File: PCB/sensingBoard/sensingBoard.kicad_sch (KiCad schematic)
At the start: 37 parts, among them J1 Conn_01x02_Socket, J2 Conn_01x03_Socket, J4 Conn_01x04_MountingPin, P1 USB_C_Plug_USB2.0, SW1 SW_Push, SW2 SW_Push, U1 AMS1117, U2 ESP32-C3-MINI-1, X1 32.768

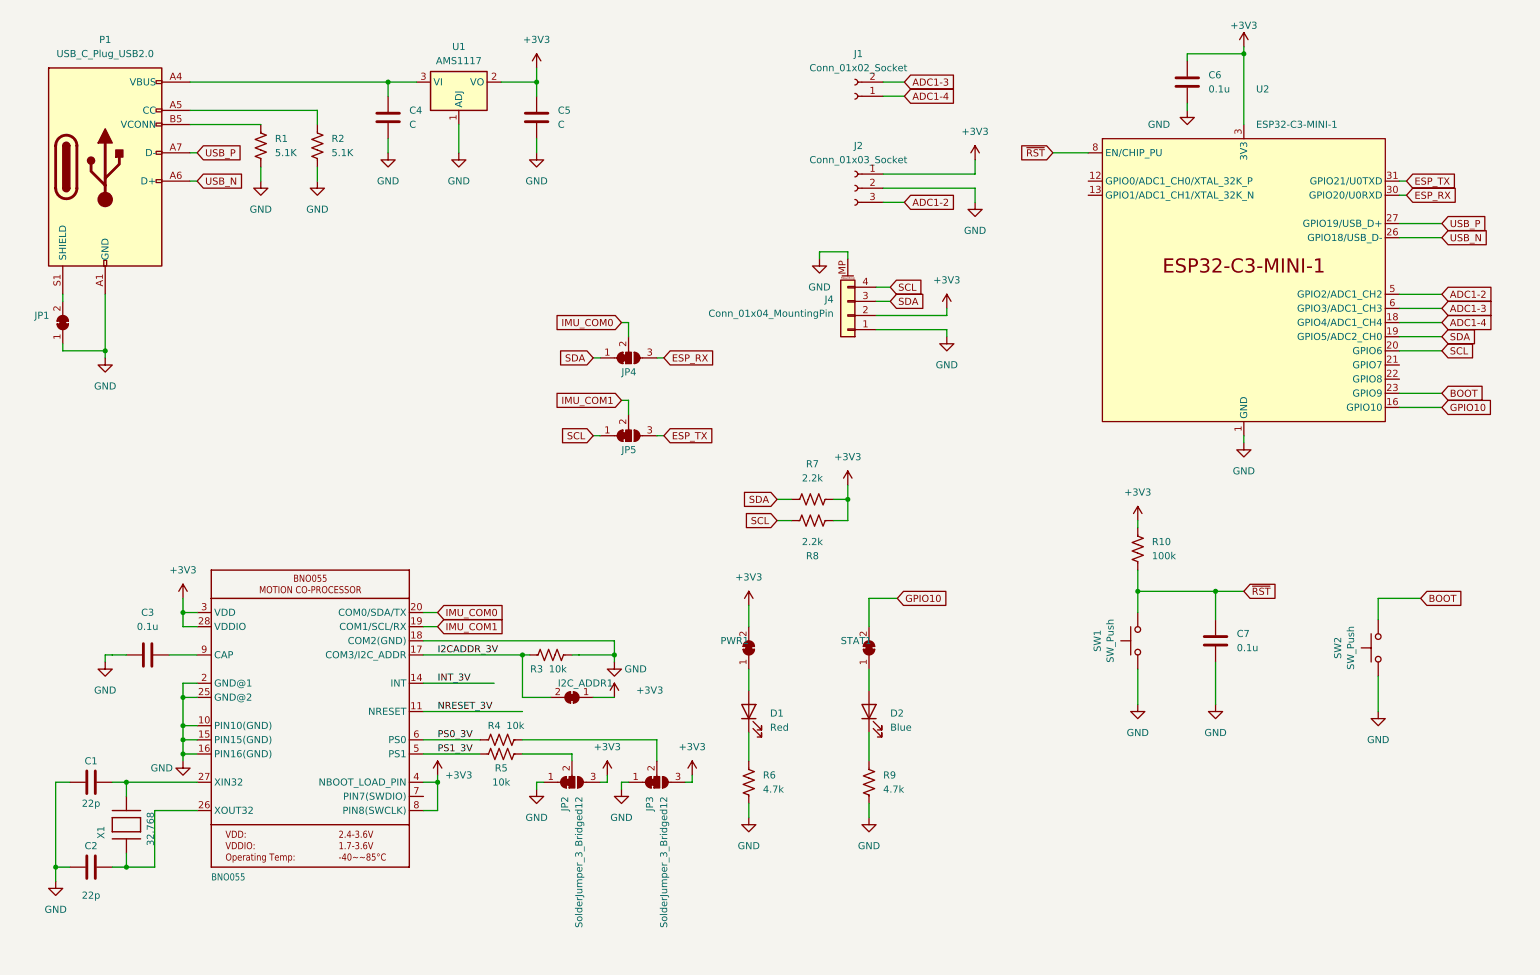
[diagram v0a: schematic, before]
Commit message: modified sensor board and wrote firmware for wireless data transfer
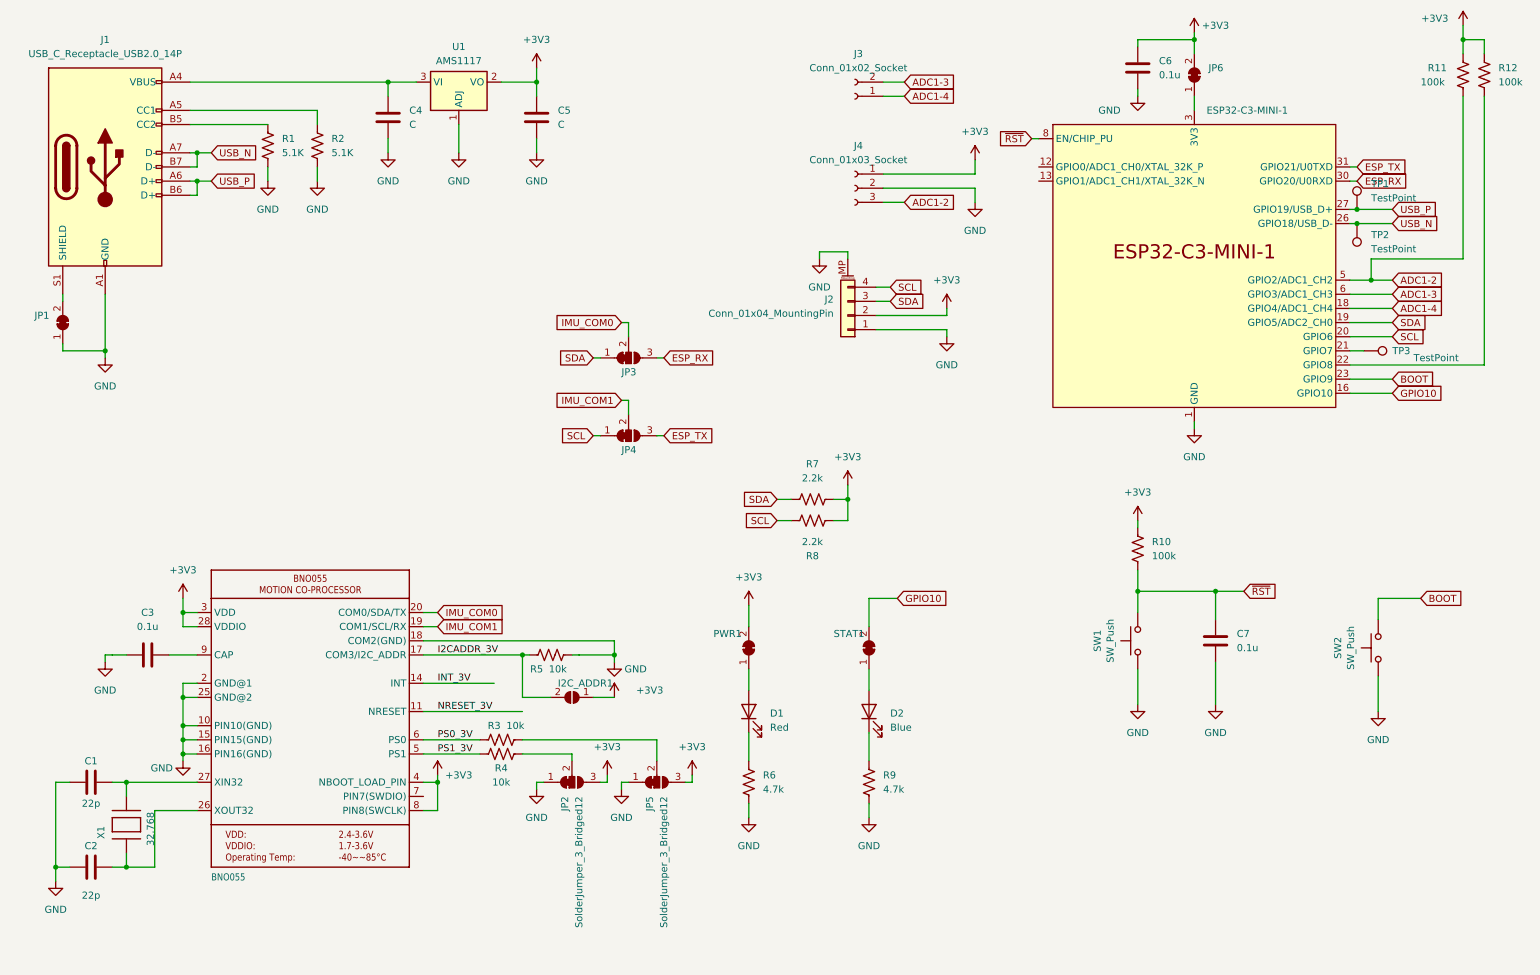
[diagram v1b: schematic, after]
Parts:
- removed P1: USB_C_Plug_USB2.0, Connector_USB:USB_C_Receptacle_GCT_USB4105-xx-A_16P_TopMnt_Horizontal, symbol Connector:USB_C_Plug_USB2.0
- added J1: USB_C_Receptacle_USB2.0_14P, Connector_USB:USB_C_Receptacle_GCT_USB4105-xx-A_16P_TopMnt_Horizontal, symbol Connector:USB_C_Receptacle_USB2.0_14P
- added JP6: ~, Jumper:SolderJumper-2_P1.3mm_Bridged_RoundedPad1.0x1.5mm, symbol Jumper:SolderJumper_2_Bridged
- added R11, R12: 100k, Resistor_SMD:R_0805_2012Metric_Pad1.20x1.40mm_HandSolder, symbol Device:R_US
- added TP1, TP2, TP3: TestPoint, TestPoint:TestPoint_Pad_D1.0mm, symbol Connector:TestPoint
- I2C_ADDR1: symbol Jumper:SolderJumper_2_Bridged -> Jumper:SolderJumper_2_Open
- JP1, PWR1, STAT1: footprint Jumper:SolderJumper-2_P1.3mm_Open_RoundedPad1.0x1.5mm -> Jumper:SolderJumper-2_P1.3mm_Bridged_RoundedPad1.0x1.5mm
- renumbered J4 to J2, J1 to J3, J2 to J4, JP4 to JP3, JP5 to JP4, JP3 to JP5, R4 to R3, R5 to R4, R3 to R5
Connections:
- net +3V3: now also JP6.2 (B), R11.1, R12.1; no longer U2.3 (3V3)
- net ADC1-2: now also R11.2
- net GND: now also J1.A1 (GND), J1.A12 (GND), J1.B1 (GND), J1.B12 (GND)
- net USB_N: now also J1.A7 (D-), J1.B7 (D-), TP2.1
- net USB_P: now also J1.A6 (D+), J1.B6 (D+), TP1.1
- net at C4.1, U1.3 (VI): now also J1.A4 (VBUS), J1.A9 (VBUS), J1.B4 (VBUS), J1.B9 (VBUS)
- net at R2.1: now also J1.A5 (CC1)
- net at R1.1: now also J1.B5 (CC2)
- net at JP1.2 (B): now also J1.S1 (SHIELD)
- net at U2.21 (GPIO7): now also TP3.1
- net at U2.22 (GPIO8): now also R12.2
- new net: JP6.1 (A), U2.3 (3V3)
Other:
- moved on the sheet: C6, R1

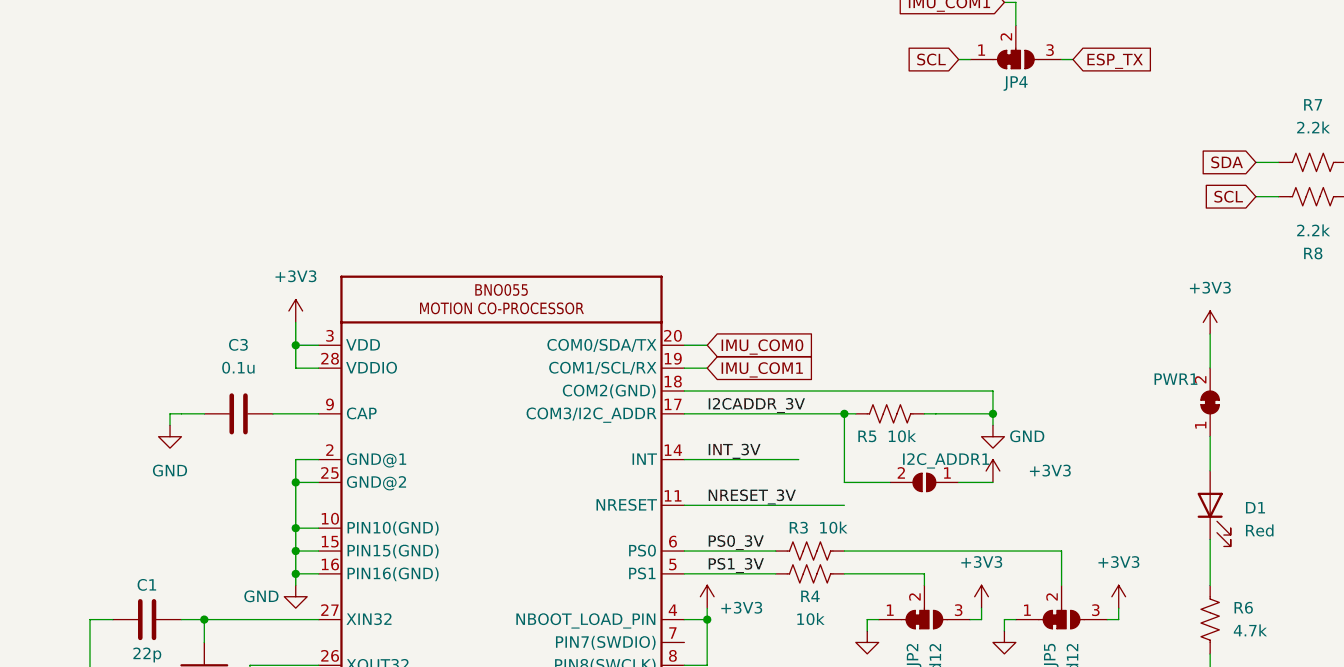
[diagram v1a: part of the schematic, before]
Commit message: gitignore for kicad backup, added pullup for nreset on imu
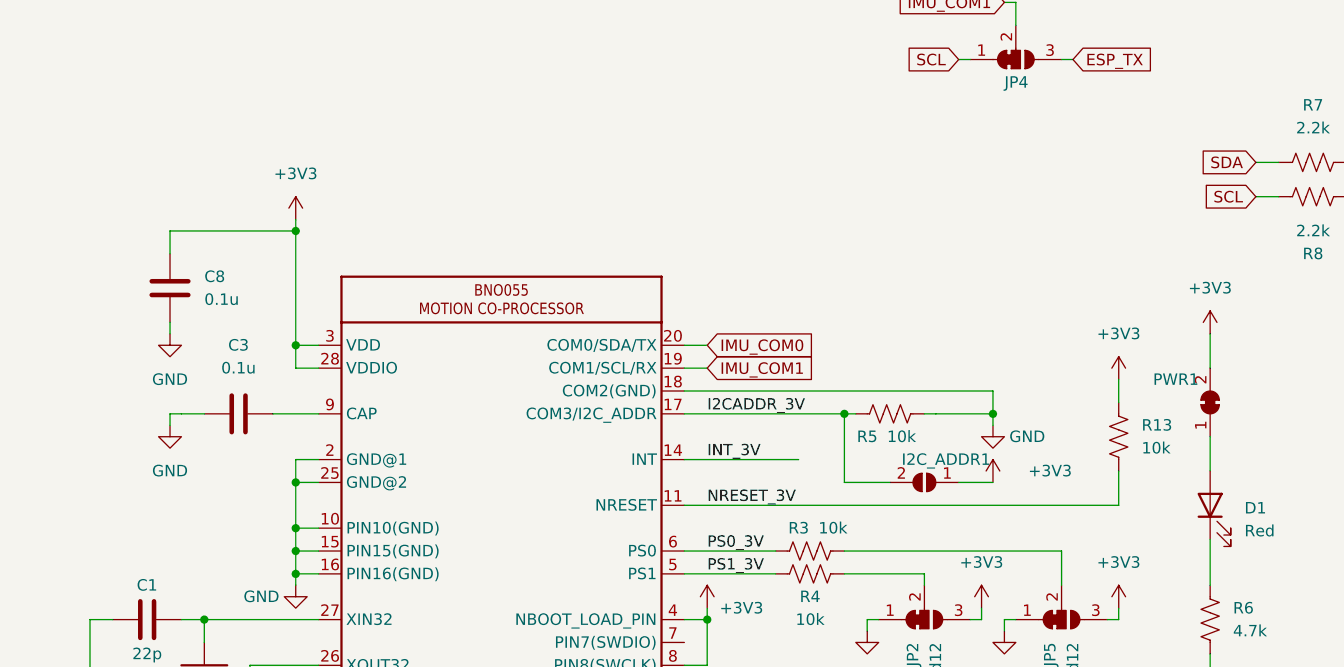
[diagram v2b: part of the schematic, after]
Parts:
- added C8: 0.1u, Capacitor_SMD:C_0805_2012Metric_Pad1.18x1.45mm_HandSolder, symbol Device:C
- added R13: 10k, Resistor_SMD:R_0805_2012Metric_Pad1.20x1.40mm_HandSolder, symbol Device:R_US
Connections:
- net +3V3: now also C8.1, R13.1
- net GND: now also C8.2
- net NRESET_3V: now also R13.2
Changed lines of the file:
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@@
   (junction (at 31.75 151.13) (diameter 0) (color 0 0 0 0)
   )
+  (junction (at 41.91 107.95) (diameter 0) (color 0 0 0 0)
+  )
   (junction (at 44.45 38.1) (diameter 0) (color 0 0 0 0)
   )
@@
     (stroke (width 0) (type default))
   )
+  (wire (pts (xy 27.94 107.95) (xy 41.91 107.95))
+    (stroke (width 0) (type default))
+  )
   (wire (pts (xy 87.63 156.21) (xy 85.09 156.21))
     (stroke (width 0.1524) (type solid))
@@
     (stroke (width 0) (type default))
   )
+  (wire (pts (xy 133.35 124.46) (xy 133.35 127))
+    (stroke (width 0) (type default))
+  )
   (wire (pts (xy 213.36 116.84) (xy 227.33 116.84))
     (stroke (width 0) (type default))
@@
     (stroke (width 0) (type default))
   )
+  (wire (pts (xy 41.91 107.95) (xy 41.91 106.68))
+    (stroke (width 0.1524) (type solid))
+  )
   (wire (pts (xy 44.45 135.89) (xy 41.91 135.89))
     (stroke (width 0.1524) (type solid))
@@
     (stroke (width 0) (type default))
   )
+  (wire (pts (xy 27.94 118.11) (xy 27.94 119.38))
+    (stroke (width 0) (type default))
+  )
   (wire (pts (xy 41.91 146.05) (xy 41.91 147.32))
     (stroke (width 0) (type default))
@@
     (stroke (width 0.1524) (type solid))
   )
+  (wire (pts (xy 133.35 134.62) (xy 133.35 138.43))
+    (stroke (width 0.1524) (type solid))
+  )
   (wire (pts (xy 44.45 146.05) (xy 41.91 146.05))
     (stroke (width 0.1524) (type solid))
@@
     (stroke (width 0) (type default))
   )
+  (wire (pts (xy 27.94 107.95) (xy 27.94 110.49))
+    (stroke (width 0) (type default))
+  )
   (wire (pts (xy 78.74 25.4) (xy 78.74 27.94))
     (stroke (width 0) (type default))
@@
     (stroke (width 0.1524) (type solid))
   )
-  (wire (pts (xy 41.91 120.65) (xy 41.91 118.11))
+  (wire (pts (xy 41.91 120.65) (xy 41.91 107.95))
     (stroke (width 0.1524) (type solid))
   )
@@
     (stroke (width 0) (type default))
   )
-  (wire (pts (xy 85.09 138.43) (xy 102.87 138.43))
+  (wire (pts (xy 85.09 138.43) (xy 133.35 138.43))
     (stroke (width 0.1524) (type solid))
   )
@@
         (path "/393f72fc-5c48-49dc-87e0-7e68fe660379"
           (reference "#PWR028") (unit 1)
+        )
+      )
+    )
+  )
+  (symbol (lib_id "Device:C") (at 27.94 114.3 0) (unit 1)
+    (in_bom yes) (on_board yes) (dnp no) (fields_autoplaced)
+    (property "Reference" "C8" (at 31.75 113.03 0)
+      (effects (font (size 1.27 1.27)) (justify left))
+    )
+    (property "Value" "0.1u" (at 31.75 115.57 0)
+      (effects (font (size 1.27 1.27)) (justify left))
+    )
+    (property "Footprint" "Capacitor_SMD:C_0805_2012Metric_Pad1.18x1.45mm_HandSolder" (at 28.9052 118.11 0)
+      (effects (font (size 1.27 1.27)) hide)
+    )
+    (property "Datasheet" "~" (at 27.94 114.3 0)
+      (effects (font (size 1.27 1.27)) hide)
+    )
+    (pin "1")
+    (pin "2")
+    (instances
+      (project "sensingBoard"
+        (path "/393f72fc-5c48-49dc-87e0-7e68fe660379"
+          (reference "C8") (unit 1)
         )
       )
@@
         (path "/393f72fc-5c48-49dc-87e0-7e68fe660379"
           (reference "R7") (unit 1)
+        )
+      )
+    )
+  )
+  (symbol (lib_id "power:GND") (at 27.94 119.38 0) (unit 1)
+    (in_bom yes) (on_board yes) (dnp no) (fields_autoplaced)
+    (property "Reference" "#PWR037" (at 27.94 125.73 0)
+      (effects (font (size 1.27 1.27)) hide)
+    )
+    (property "Value" "GND" (at 27.94 124.46 0)
+      (effects (font (size 1.27 1.27)))
+    )
+    (property "Footprint" "" (at 27.94 119.38 0)
+      (effects (font (size 1.27 1.27)) hide)
+    )
+    (property "Datasheet" "" (at 27.94 119.38 0)
+      (effects (font (size 1.27 1.27)) hide)
+    )
+    (pin "1")
+    (instances
+      (project "sensingBoard"
+        (path "/393f72fc-5c48-49dc-87e0-7e68fe660379"
+          (reference "#PWR037") (unit 1)
         )
       )
@@
     )
   )
+  (symbol (lib_id "power:+3V3") (at 133.35 124.46 0) (unit 1)
+    (in_bom yes) (on_board yes) (dnp no) (fields_autoplaced)
+    (property "Reference" "#PWR036" (at 133.35 128.27 0)
+      (effects (font (size 1.27 1.27)) hide)
+    )
+    (property "Value" "+3V3" (at 133.35 119.38 0)
+      (effects (font (size 1.27 1.27)))
+    )
+    (property "Footprint" "" (at 133.35 124.46 0)
+      (effects (font (size 1.27 1.27)) hide)
+    )
+    (property "Datasheet" "" (at 133.35 124.46 0)
+      (effects (font (size 1.27 1.27)) hide)
+    )
+    (pin "1")
+    (instances
+      (project "sensingBoard"
+        (path "/393f72fc-5c48-49dc-87e0-7e68fe660379"
+          (reference "#PWR036") (unit 1)
+        )
+      )
+    )
+  )
   (symbol (lib_id "power:+3V3") (at 271.78 15.24 0) (unit 1)
     (in_bom yes) (on_board yes) (dnp no)
@@
     )
   )
-  (symbol (lib_id "power:+3V3") (at 41.91 118.11 0) (unit 1)
-    (in_bom yes) (on_board yes) (dnp no) (fields_autoplaced)
-    (property "Reference" "#PWR04" (at 41.91 121.92 0)
-      (effects (font (size 1.27 1.27)) hide)
-    )
-    (property "Value" "+3V3" (at 41.91 113.03 0)
-      (effects (font (size 1.27 1.27)))
-    )
-    (property "Footprint" "" (at 41.91 118.11 0)
-      (effects (font (size 1.27 1.27)) hide)
-    )
-    (property "Datasheet" "" (at 41.91 118.11 0)
+  (symbol (lib_id "power:+3V3") (at 41.91 106.68 0) (unit 1)
+    (in_bom yes) (on_board yes) (dnp no) (fields_autoplaced)
+    (property "Reference" "#PWR04" (at 41.91 110.49 0)
+      (effects (font (size 1.27 1.27)) hide)
+    )
+    (property "Value" "+3V3" (at 41.91 101.6 0)
+      (effects (font (size 1.27 1.27)))
+    )
+    (property "Footprint" "" (at 41.91 106.68 0)
+      (effects (font (size 1.27 1.27)) hide)
+    )
+    (property "Datasheet" "" (at 41.91 106.68 0)
       (effects (font (size 1.27 1.27)) hide)
     )
@@
         )
       )
+    )
+  )
+  (symbol (lib_id "Device:R_US") (at 133.35 130.81 0) (unit 1)
+    (in_bom yes) (on_board yes) (dnp no) (fields_autoplaced)
+    (property "Reference" "R13" (at 135.89 129.54 0)
+      (effects (font (size 1.27 1.27)) (justify left))
+    )
+    (property "Value" "10k" (at 135.89 132.08 0)
+      (effects (font (size 1.27 1.27)) (justify left))
+    )
+    (property "Footprint" "Resistor_SMD:R_0805_2012Metric_Pad1.20x1.40mm_HandSolder" (at 134.366 131.064 90)
+      (effects (font (size 1.27 1.27)) hide)
+    )
+    (property "Datasheet" "~" (at 133.35 130.81 0)
+      (effects (font (size 1.27 1.27)) hide)
+    )
+    (pin "1")
+    (pin "2")
+    (instances
+      (project "sensingBoard"
+        (path "/393f72fc-5c48-49dc-87e0-7e68fe660379"
+          (reference "R13") (unit 1)
+        )
+      )
